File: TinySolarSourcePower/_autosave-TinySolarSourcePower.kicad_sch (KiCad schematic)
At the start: 16 parts, among them J1 Conn_01x02_Pin, J2 Conn_01x02_Pin, J3 Conn_01x02_Pin, J4 Conn_01x02_Pin, Q1 2N7002, U1 AP3015AKTR-G1

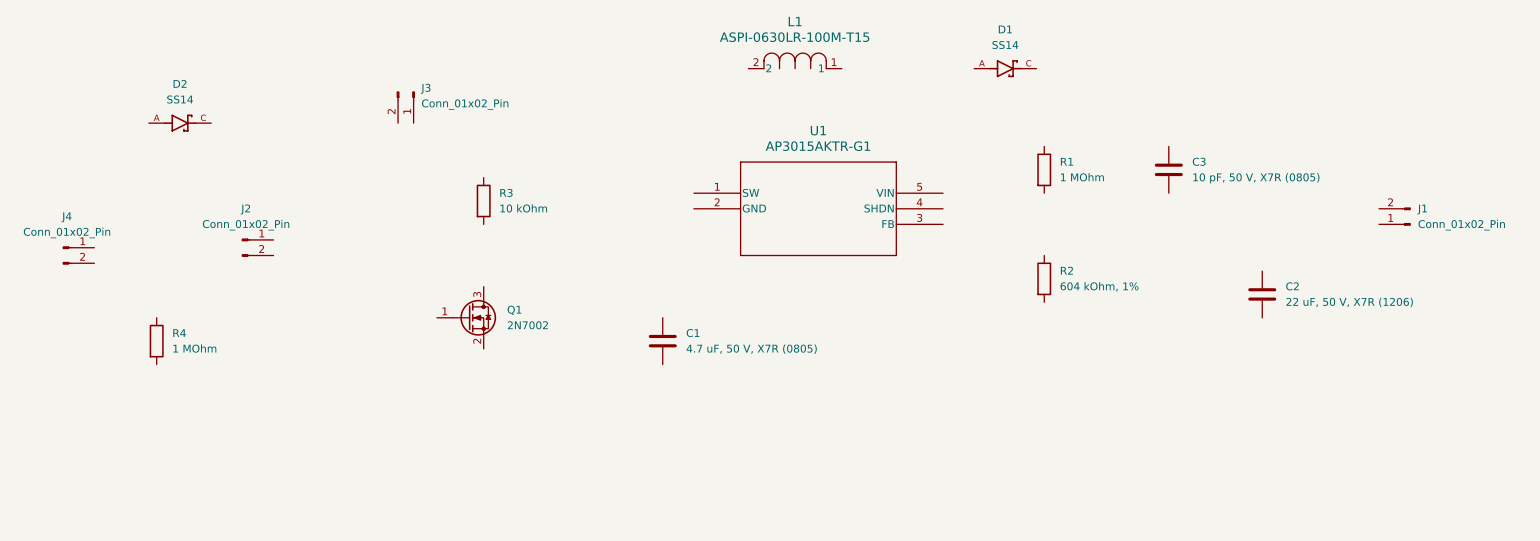
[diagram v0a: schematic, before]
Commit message: add values for elemnts and add wires
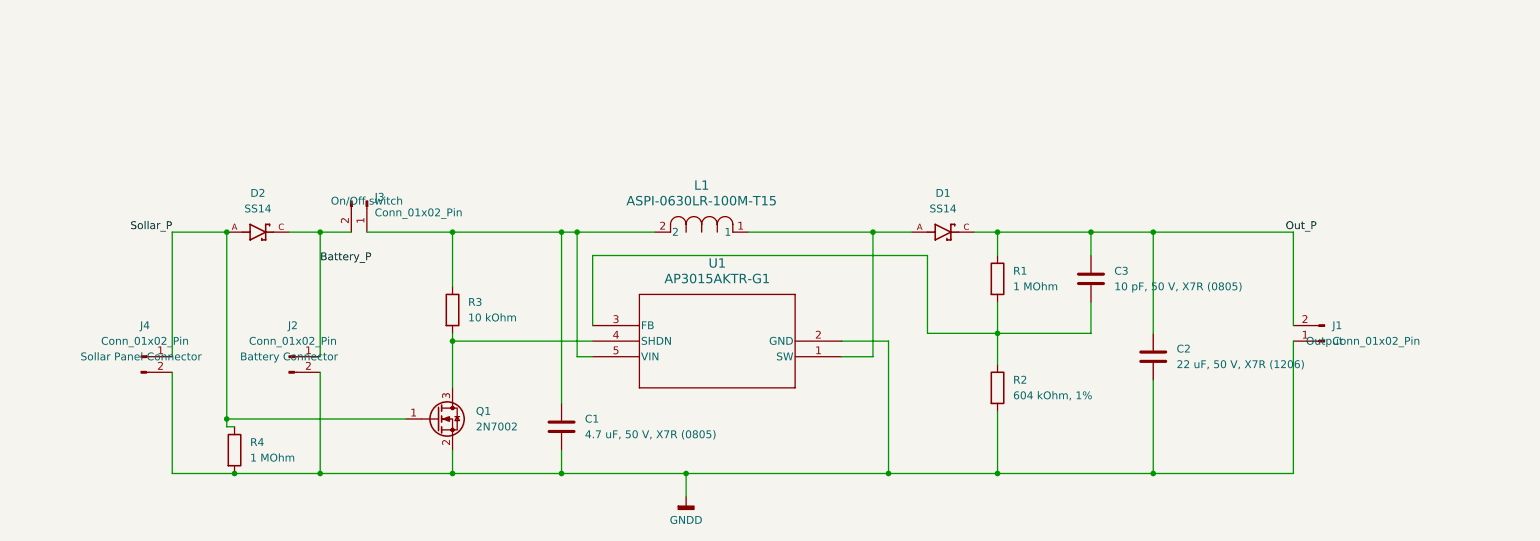
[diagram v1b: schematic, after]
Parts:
- J1: Short description (none) -> Output
- J2: Short description (none) -> Battery Connector
- J3: Short description (none) -> On/Off switch
- J4: Short description (none) -> Sollar Panel Connector
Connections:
- net Battery_P: now reaches J2.1 (Pin_1)
- net Battery_P: now also D2.C, J3.2 (Pin_2)
- net GNDD: now reaches J2.2 (Pin_2)
- net GNDD: now also C1.2, C2.2, J1.1 (Pin_1), J4.2 (Pin_2), Q1.2 (S), R2.2, R4.2, U1.2 (GND)
- net Sollar_P: now reaches D2.A
- net Sollar_P: now also J4.1 (Pin_1), Q1.1 (G), R4.1
- net at U1.1 (SW): now also D1.A, L1.1
- net at U1.3 (FB): now also C3.2, R1.2, R2.1
- net at U1.4 (SHDN): now also Q1.3 (D), R3.2
- net at U1.5 (VIN): now also C1.1, J3.1 (Pin_1), L1.2, R3.1
- net Out_P: now reaches J1.2 (Pin_2)
- net Out_P: now also C2.1, C3.1, D1.C, R1.1
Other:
- moved on the sheet: C1, C2, C3, D1, D2, J1, J2, J3, J4, L1, Q1, R1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
